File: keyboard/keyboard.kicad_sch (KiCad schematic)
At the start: 144 parts, among them J1 USB_C_Receptacle, J4 ISP, SW1 RESET, U1 ATmega32U4-A, Y1 16MHz

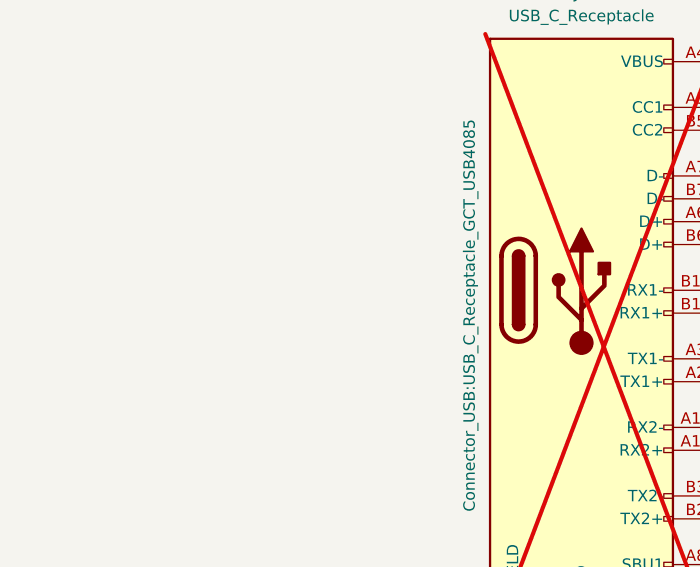
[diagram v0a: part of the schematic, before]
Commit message: New enclousre and fix for PCB
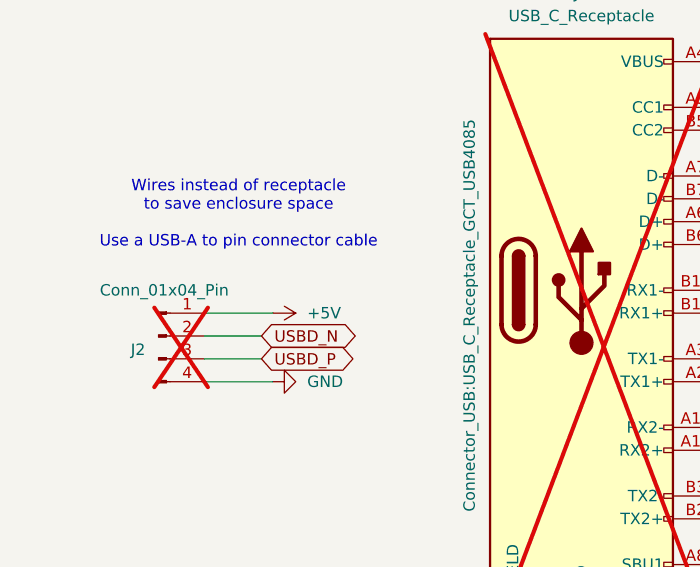
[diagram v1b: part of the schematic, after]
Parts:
- added J2: Conn_01x04_Pin, Connector_PinHeader_2.54mm:PinHeader_1x04_P2.54mm_Vertical, symbol Connector:Conn_01x04_Pin
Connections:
- net +5V: now also J2.1 (Pin_1)
- net GND: now also J2.4 (Pin_4)
- net USBD_N: now also J2.2 (Pin_2)
- net USBD_P: now also J2.3 (Pin_3)
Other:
- note added: "Wires instead of receptacle to save enclosure space Use a USB-A to pin connector cable"
